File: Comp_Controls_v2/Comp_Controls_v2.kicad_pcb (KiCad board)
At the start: 2 copper layers, 35 parts

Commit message: Add edge cuts and copper fill
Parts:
- moved ANEMOMETER1 5.34 mm to (129.7, 86.0)
- moved C1 5.34 mm to (166.7, 112.7)
- moved C6 5.34 mm to (166.0, 121.6)
- moved C9 5.34 mm to (155.3, 64.3)
- moved StepDownChip1 5.34 mm to (163.7, 124.7)
- moved XBEE1 5.34 mm to (132.8, 119.8)
- moved 5V_BULK1 5.34 mm to (144.3, 48.0)
- moved TeensyC0.1 5.34 mm to (179.8, 91.1)
- moved 5V_BULK3 5.34 mm to (129.3, 48.0)
- moved 5V_MID2 5.34 mm to (125.7, 59.4)
- moved 3.3V_BULK1 5.34 mm to (178.4, 63.6)
- moved 3.3V_SYS1 5.34 mm to (179.6, 52.0)
- moved C11 5.34 mm to (146.4, 64.1)
- moved C12 5.34 mm to (163.9, 64.3)
- moved C2 5.34 mm to (166.5, 116.5)
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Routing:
- added copper zone on F.Cu, net (none)
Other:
- board outline added: 67.5 x 99 mm
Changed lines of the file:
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@@
 	(footprint "MountingHole:MountingHole_3.2mm_M3"
 		(layer "F.Cu")
-		(at 138.98 86)
+		(at 140.87 81.01)
 		(descr "Mounting Hole 3.2mm, M3, no annular, generated by kicad-footprint-generator mountinghole.py")
 		(tags "mountinghole M3")
@@
 	(footprint "Comp_Controls_v2:CAP_CL10B_01uf_0603"
 		(layer "F.Cu")
-		(at 164.6 121.44 -90)
+		(at 166.49 116.45 -90)
 		(property "Reference" "C2"
 			(at -0.21 -1.05 90)
@@
 	(footprint "Comp_Controls_v2:CAP_CL10B_01uf_0603"
 		(layer "F.Cu")
-		(at 144.54 69.05 90)
+		(at 146.43 64.06 90)
 		(property "Reference" "C11"
 			(at 1.96 -0.03 180)
@@
 	(footprint "Comp_Controls_v2:CAP_CL10B_01uf_0603"
 		(layer "F.Cu")
-		(at 148.37 126.83)
+		(at 150.26 121.84)
 		(property "Reference" "C4"
 			(at -0.21 -1.05 0)
@@
 	(footprint "Comp_Controls_v2:CAP_CL10B_01uf_0603"
 		(layer "F.Cu")
-		(at 177.9 96.06)
+		(at 179.79 91.07)
 		(property "Reference" "TeensyC0.1"
 			(at -0.21 -1.05 0)
@@
 	(footprint "Comp_Controls_v2:CAP_C3225_47uf_1210"
 		(layer "F.Cu")
-		(at 148.37 131.13 90)
+		(at 150.26 126.14 90)
 		(tags "C3225X5R1A476M250AC ")
 		(property "Reference" "C5"
@@
 			(polygon
 				(pts
-					(xy 146.973 132.1841) (xy 146.973 130.0759) (xy 149.767 130.0759) (xy 149.767 132.1841)
+					(xy 148.863 127.1941) (xy 148.863 125.0859) (xy 151.657 125.0859) (xy 151.657 127.1941)
 				)
 			)
@@
 	(footprint "Comp_Controls_v2:CAP_CL10B_01uf_0603"
 		(layer "F.Cu")
-		(at 166.36 126.52 90)
+		(at 168.25 121.53 90)
 		(property "Reference" "C3"
 			(at -2.13 0.04 180)
@@
 	(footprint "Connector_Dsub:DSUB-9_Socket_Vertical_P2.77x2.84mm_MountingHoles"
 		(layer "F.Cu")
-		(at 173.53 119.42 90)
+		(at 175.42 114.43 90)
 		(descr "9-pin D-Sub connector, straight/vertical, THT-mount, socket (female), pitch 2.77x2.84mm, distance of mounting holes 25mm, see https://disti-assets.s3.amazonaws.com/tonar/files/datasheets/16730.pdf")
 		(tags "9-pin D-Sub connector straight vertical THT socket pitch 2.77x2.84mm mounting holes distance 25mm")
@@
 	(footprint "Comp_Controls_v2:CAP_CL10B_01uf_0603"
 		(layer "F.Cu")
-		(at 164.14 126.62 90)
+		(at 166.03 121.63 90)
 		(property "Reference" "C6"
 			(at -2.03 -0.09 180)
@@
 	(footprint "MountingHole:MountingHole_3.2mm_M3"
 		(layer "F.Cu")
-		(at 157.64 137.57)
+		(at 159.53 132.58)
 		(descr "Mounting Hole 3.2mm, M3, no annular, generated by kicad-footprint-generator mountinghole.py")
 		(tags "mountinghole M3")
@@
 	(footprint "Comp_Controls_v2:CAP_CL21A_10uf_0805"
 		(layer "F.Cu")
-		(at 177.435 61.85)
+		(at 179.325 56.86)
 		(property "Reference" "3.3V_MID1"
 			(at -0.44 -1.3 0)
@@
 	(footprint "Comp_Controls_v2:CAP_CL10B_01uf_0603"
 		(layer "F.Cu")
-		(at 153.39 69.26 90)
+		(at 155.28 64.27 90)
 		(property "Reference" "C9"
 			(at 1.84 -0.07 180)
@@
 	(footprint "Comp_Controls_v2:MODULE_DEV-15583"
 		(layer "F.Cu")
-		(at 162.56 85.28 -90)
+		(at 164.45 80.29 -90)
 		(property "Reference" "TEENSY1"
 			(at -5.715 -19.685 90)
@@
 	(footprint "Comp_Controls_v2:CAP_CL10B_01uf_0603"
 		(layer "F.Cu")
-		(at 127.9 64.28 -90)
+		(at 129.79 59.29 -90)
 		(property "Reference" "5V_LOW1"
 			(at -1.98 -0.02 180)
@@
 	(footprint "Comp_Controls_v2:CAP_CL10B_01uf_0603"
 		(layer "F.Cu")
-		(at 128.27 86.02 180)
+		(at 130.16 81.03 180)
 		(property "Reference" "C10"
 			(at -0.21 -1.05 0)
@@
 	(footprint "Comp_Controls_v2:CAP_EEE1A_1000uf"
 		(layer "F.Cu")
-		(at 127.46 52.99 180)
+		(at 129.35 48 180)
 		(property "Reference" "5V_BULK3"
 			(at -0.375 -6.535 0)
@@
 	(footprint "Comp_Controls_v2:HARWIN_M20-7832046"
 		(layer "F.Cu")
-		(at 147.18 99.89)
+		(at 149.07 94.9)
 		(property "Reference" "HEADERS1"
 			(at -22.435 -3.635 0)
@@
 	(footprint "Comp_Controls_v2:CAP_CL32A_22uf_1210"
 		(layer "F.Cu")
-		(at 123.78 64.34 -90)
+		(at 125.67 59.35 -90)
 		(property "Reference" "5V_MID2"
 			(at -2.85 -0.04 180)
@@
 	(footprint "Comp_Controls_v2:XBee"
 		(layer "F.Cu")
-		(at 130.94 124.84 180)
+		(at 132.83 119.85 180)
 		(property "Reference" "XBEE1"
 			(at 0 -0.5 180)
@@
 			(polygon
 				(pts
-					(xy 145.94 140.84) (xy 120.94 140.84) (xy 120.94 104.84) (xy 145.94 104.84)
+					(xy 147.83 135.85) (xy 122.83 135.85) (xy 122.83 99.85) (xy 147.83 99.85)
 				)
 			)
@@
 	(footprint "Comp_Controls_v2:CAP_EEE1A_1000uf"
 		(layer "F.Cu")
-		(at 142.38 53 180)
+		(at 144.27 48.01 180)
 		(property "Reference" "5V_BULK1"
 			(at -0.375 -6.535 0)
@@
 	(footprint "Comp_Controls_v2:B3B-XH-A"
 		(layer "F.Cu")
-		(at 157.55 69.318333 -90)
+		(at 159.44 64.328333 -90)
 		(property "Reference" "RUDDER1"
 			(at -6.16 -0.305 180)
@@
 	(footprint "Comp_Controls_v2:B4B-XH-A"
 		(layer "F.Cu")
-		(at 127.8175 90.95)
+		(at 129.7075 85.96)
 		(property "Reference" "ANEMOMETER1"
 			(at -7.8175 0.16 90)
@@
 	(footprint "MountingHole:MountingHole_3.2mm_M3"
 		(layer "F.Cu")
-		(at 177.9 103.97)
+		(at 179.79 98.98)
 		(descr "Mounting Hole 3.2mm, M3, no annular, generated by kicad-footprint-generator mountinghole.py")
 		(tags "mountinghole M3")
@@
 	(footprint "Connector_Molex:Molex_Mini-Fit_Jr_5566-06A_2x03_P4.20mm_Vertical"
 		(layer "F.Cu")
-		(at 163.68 56.97 180)
+		(at 165.57 51.98 180)
 		(descr "Molex Mini-Fit Jr. Power Connectors, old mpn/engineering number: 5566-06A, example for new mpn: 39-28-x06x, 3 Pins per row, Mounting:  (http://www.molex.com/pdm_docs/sd/039281043_sd.pdf), generated with kicad-footprint-generator")
 		(tags "connector Molex Mini-Fit_Jr vertical")
@@
 	(footprint "Comp_Controls_v2:CAP_87510_220uf"
 		(layer "F.Cu")
-		(at 176.54 68.55 90)
+		(at 178.43 63.56 90)
 		(property "Reference" "3.3V_BULK1"
 			(at -0.6 -4.708 90)
@@
 	(footprint "Comp_Controls_v2:B3B-XH-A"
 		(layer "F.Cu")
-		(at 140.05 69.13 -90)
+		(at 141.94 64.14 -90)
 		(property "Reference" "5v_extra1"
 			(at -6.44 -0.095 180)
@@
 	(footprint "Comp_Controls_v2:MAX3323EEPE+"
 		(layer "F.Cu")
-		(at 161.85 129.65 180)
+		(at 163.74 124.66 180)
 		(tags "max3323eepe+ ")
 		(property "Reference" "StepDownChip1"
@@
 	(footprint "Comp_Controls_v2:CAP_CL10B_01uf_0603"
 		(layer "F.Cu")
-		(at 128.03 95.13 180)
+		(at 129.92 90.14 180)
 		(property "Reference" "C8"
 			(at -0.21 -1.05 0)
@@
 	(footprint "Comp_Controls_v2:B4B-XH-A"
 		(layer "F.Cu")
-		(at 127.84 81.625)
+		(at 129.73 76.635)
 		(property "Reference" "3.3v_extra1"
 			(at -7.99 -1.135 90)
@@
 	(footprint "Connector_Molex:Molex_Mini-Fit_Jr_5566-04A_2x02_P4.20mm_Vertical"
 		(layer "F.Cu")
-		(at 177.72 57.01 180)
+		(at 179.61 52.02 180)
 		(descr "Molex Mini-Fit Jr. Power Connectors, old mpn/engineering number: 5566-04A, example for new mpn: 39-28-x04x, 2 Pins per row, Mounting:  (http://www.molex.com/pdm_docs/sd/039281043_sd.pdf), generated with kicad-footprint-generator")
 		(tags "connector Molex Mini-Fit_Jr vertical")
@@
 	(footprint "Comp_Controls_v2:B3B-XH-A"
 		(layer "F.Cu")
-		(at 166.3 69.4125 -90)
+		(at 168.19 64.4225 -90)
 		(property "Reference" "SAIL1"
 			(at -6.29 0.005 180)
@@
 	(footprint "Comp_Controls_v2:CAP_CL10B_01uf_0603"
 		(layer "F.Cu")
-		(at 135.44 66.88 90)
+		(at 137.33 61.89 90)
 		(property "Reference" "C7"
 			(at 1.89 -0.02 180)
@@
 	(footprint "Comp_Controls_v2:CAP_CL10B_01uf_0603"
 		(layer "F.Cu")
-		(at 164.79 117.65 90)
+		(at 166.68 112.66 90)
 		(property "Reference" "C1"
 			(at -0.21 -1.05 90)
@@
 	(footprint "Comp_Controls_v2:B3B-XH-A"
 		(layer "F.Cu")
-		(at 148.8 69.224167 -90)
+		(at 150.69 64.234167 -90)
 		(property "Reference" "JIB1"
 			(at -6.204167 -0.06 180)
@@
 	(footprint "Comp_Controls_v2:CAP_CL10B_01uf_0603"
 		(layer "F.Cu")
-		(at 161.98 69.25 90)
+		(at 163.87 64.26 90)
 		(property "Reference" "C12"
 			(at 1.9 -0.05 180)
@@
 		(embedded_fonts no)
 	)
+	(gr_rect
+		(start 119.5 39.5)
+		(end 187 138.5)
+		(stroke
+			(width 0.05)
+			(type default)
+		)
+		(fill no)
+		(layer "Edge.Cuts")
+	)
+	(zone
+		(net 0)
+		(net_name "")
+		(layer "F.Cu")
+		(hatch edge 0.5)
+		(connect_pads
+			(clearance 0.5)
+		)
+		(min_thickness 0.25)
+		(filled_areas_thickness no)
+		(fill
+			(thermal_gap 0.5)
+			(thermal_bridge_width 0.5)
+			(island_removal_mode 1)
+			(island_area_min 10)
+		)
+		(polygon
+			(pts
+				(xy 116 36.5) (xy 190.5 36.5) (xy 190.5 142.5) (xy 116.5 142.5)
+			)
+		)
+	)
 	(embedded_fonts no)

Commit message: finished ground vias
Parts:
- moved C2 4.27 mm to (166.3, 112.2), turned to 90 degrees
- moved C1 3.38 mm to (166.0, 116.0)
- renumbered JIB1 to JIB, RUDDER1 to RUDDER, SAIL1 to SAIL
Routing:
- net GND: track 0.00 -> 23.5 mm, vias 0 -> 16
- net Net-(VectorNavInput1-Pad1): track 0.00 -> 11.5 mm
- net Net-(StepDownChip1-C1+): track 0.00 -> 5.48 mm
- net Net-(StepDownChip1-C1-): track 0.00 -> 4.99 mm
- net Net-(StepDownChip1-V-): track 0.00 -> 3.00 mm
- net Net-(StepDownChip1-V+): track 0.00 -> 2.82 mm
- net Net-(StepDownChip1-C2-): track 0.00 -> 2.53 mm
- net Net-(StepDownChip1-C2+): track 0.00 -> 2.36 mm

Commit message: Add tracks
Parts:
- moved C8 1.74 mm to (128.2, 90.5)
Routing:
- net WindData1: track 0.00 -> 40.1 mm
- net WindData0: track 0.00 -> 35.0 mm
- net 5v_extra: track 0.00 -> 26.8 mm
- net Extra41: track 0.00 -> 23.9 mm
- net Extra40: track 0.00 -> 18.8 mm
- net Rudder: track 0.00 -> 11.8 mm
- net JIB: track 0.00 -> 8.17 mm
- net Sail: track 0.00 -> 7.29 mm
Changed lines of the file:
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@@
 	(footprint "Comp_Controls_v2:CAP_CL10B_01uf_0603"
 		(layer "F.Cu")
-		(at 129.92 90.14 180)
+		(at 128.22 90.5 180)
 		(property "Reference" "C8"
 			(at -0.21 -1.05 0)
@@
 	)
 	(segment
-		(start 129.14 90.14)
-		(end 128.13 90.14)
+		(start 127.44 90.5)
+		(end 126.43 90.5)
 		(width 0.2)
 		(layer "F.Cu")
@@
 	)
 	(segment
-		(start 128.13 90.14)
-		(end 128.12 90.15)
+		(start 126.43 90.5)
+		(end 126.42 90.51)
 		(width 0.2)
 		(layer "F.Cu")
@@
 	)
 	(via
-		(at 128.12 90.15)
+		(at 126.42 90.51)
 		(size 0.6)
 		(drill 0.3)
@@
 	)
 	(segment
+		(start 131.904 73.736)
+		(end 149.414 73.736)
+		(width 0.2)
+		(layer "F.Cu")
+		(net 3)
+	)
+	(segment
+		(start 149.414 73.736)
+		(end 150.48 72.67)
+		(width 0.2)
+		(layer "F.Cu")
+		(net 3)
+	)
+	(segment
+		(start 128.48 77.16)
+		(end 131.904 73.736)
+		(width 0.2)
+		(layer "F.Cu")
+		(net 3)
+	)
+	(segment
+		(start 130.98 77.16)
+		(end 135.47 72.67)
+		(width 0.2)
+		(layer "B.Cu")
+		(net 4)
+	)
+	(segment
+		(start 135.47 72.67)
+		(end 147.94 72.67)
+		(width 0.2)
+		(layer "B.Cu")
+		(net 4)
+	)
+	(segment
+		(start 163.55 70.5)
+		(end 165.72 72.67)
+		(width 0.2)
+		(layer "F.Cu")
+		(net 7)
+	)
+	(segment
+		(start 143.14 66.64)
+		(end 147 70.5)
+		(width 0.2)
+		(layer "F.Cu")
+		(net 7)
+	)
+	(segment
+		(start 141.415 66.64)
+		(end 143.14 66.64)
+		(width 0.2)
+		(layer "F.Cu")
+		(net 7)
+	)
+	(segment
+		(start 147 70.5)
+		(end 163.55 70.5)
+		(width 0.2)
+		(layer "F.Cu")
+		(net 7)
+	)
+	(segment
+		(start 134.9725 90.5)
+		(end 149.75 90.5)
+		(width 0.2)
+		(layer "B.Cu")
+		(net 8)
+	)
+	(segment
+		(start 156.01 90.5)
+		(end 158.05 90.5)
+		(width 0.2)
+		(layer "B.Cu")
+		(net 8)
+	)
+	(segment
+		(start 149.75 90.5)
+		(end 152.88 93.63)
+		(width 0.2)
+		(layer "B.Cu")
+		(net 8)
+	)
+	(segment
+		(start 130.9575 86.485)
+		(end 134.9725 90.5)
+		(width 0.2)
+		(layer "B.Cu")
+		(net 8)
+	)
+	(segment
+		(start 158.05 90.5)
+		(end 160.64 87.91)
+		(width 0.2)
+		(layer "B.Cu")
+		(net 8)
+	)
+	(segment
+		(start 152.88 93.63)
+		(end 156.01 90.5)
+		(width 0.2)
+		(layer "B.Cu")
+		(net 8)
+	)
+	(segment
+		(start 159.59 91.5)
+		(end 163.18 87.91)
+		(width 0.2)
+		(layer "F.Cu")
+		(net 9)
+	)
+	(segment
+		(start 153.29 91.5)
+		(end 155.42 93.63)
+		(width 0.2)
+		(layer "F.Cu")
+		(net 9)
+	)
+	(segment
+		(start 157.5 91.5)
+		(end 159.59 91.5)
+		(width 0.2)
+		(layer "F.Cu")
+		(net 9)
+	)
+	(segment
+		(start 157.5 91.55)
+		(end 157.5 91.5)
+		(width 0.2)
+		(layer "F.Cu")
+		(net 9)
+	)
+	(segment
+		(start 128.4575 86.485)
+		(end 133.4725 91.5)
+		(width 0.2)
+		(layer "F.Cu")
+		(net 9)
+	)
+	(segment
+		(start 133.4725 91.5)
+		(end 153.29 91.5)
+		(width 0.2)
+		(layer "F.Cu")
+		(net 9)
+	)
+	(segment
+		(start 155.42 93.63)
+		(end 157.5 91.55)
+		(width 0.2)
+		(layer "F.Cu")
+		(net 9)
+	)
+	(segment
 		(start 164.03 116.75)
 		(end 163.74 117.04)
@@
 	)
 	(segment
+		(start 164.5 70.5)
+		(end 166.09 70.5)
+		(width 0.2)
+		(layer "F.Cu")
+		(net 18)
+	)
+	(segment
+		(start 160.828333 66.828333)
+		(end 164.5 70.5)
+		(width 0.2)
+		(layer "F.Cu")
+		(net 18)
+	)
+	(segment
+		(start 166.09 70.5)
+		(end 168.26 72.67)
+		(width 0.2)
+		(layer "F.Cu")
+		(net 18)
+	)
+	(segment
+		(start 158.915 66.828333)
+		(end 160.828333 66.828333)
+		(width 0.2)
+		(layer "F.Cu")
+		(net 18)
+	)
+	(segment
+		(start 167.2425 66.5)
+		(end 167 66.5)
+		(width 0.2)
+		(layer "F.Cu")
+		(net 29)
+	)
+	(segment
+		(start 167.665 69.535)
+		(end 170.8 72.67)
+		(width 0.2)
+		(layer "B.Cu")
+		(net 29)
+	)
+	(segment
+		(start 167.665 66.9225)
+		(end 167.665 69.535)
+		(width 0.2)
+		(layer "B.Cu")
+		(net 29)
+	)
+	(segment
+		(start 150.165 66.734167)
+		(end 150.165 67.275)
+		(width 0.2)
+		(layer "B.Cu")
+		(net 32)
+	)
+	(segment
+		(start 150.165 67.275)
+		(end 155.56 72.67)
+		(width 0.2)
+		(layer "B.Cu")
+		(net 32)
+	)
+	(segment

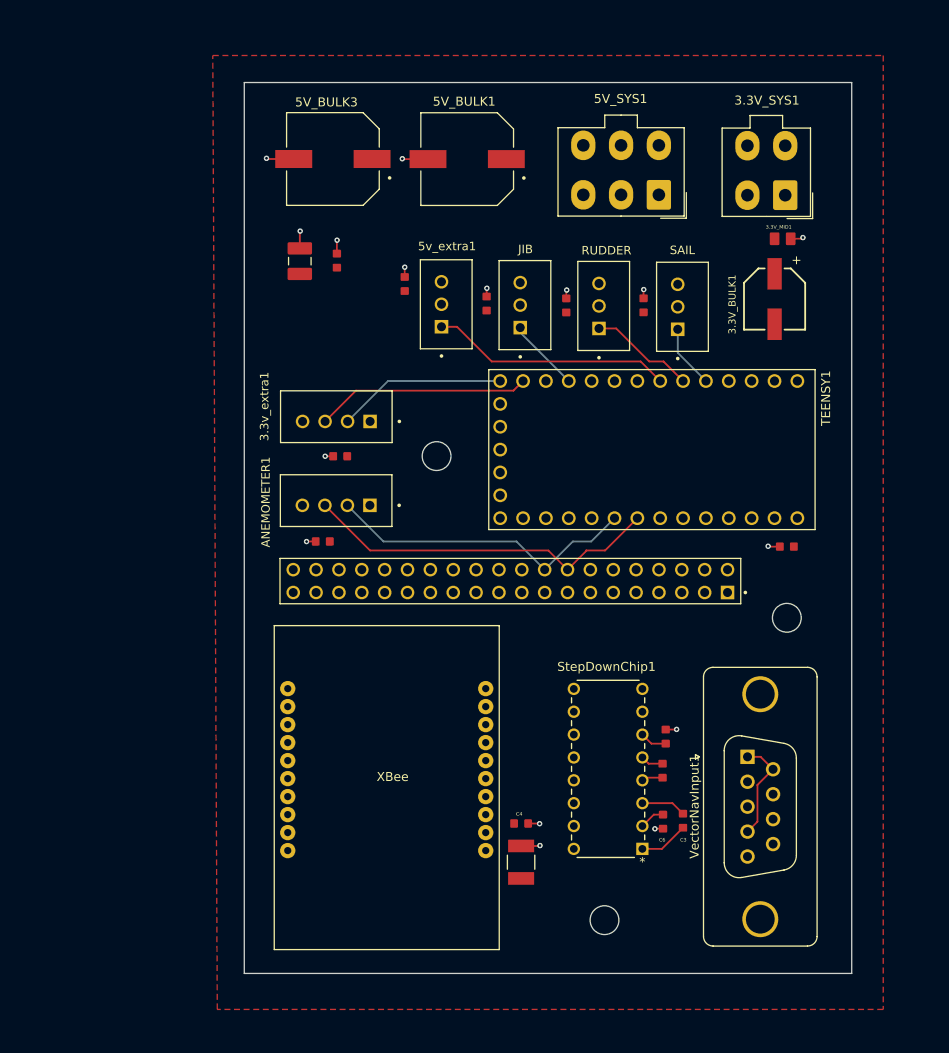
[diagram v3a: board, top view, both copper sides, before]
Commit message: changed mounting holes
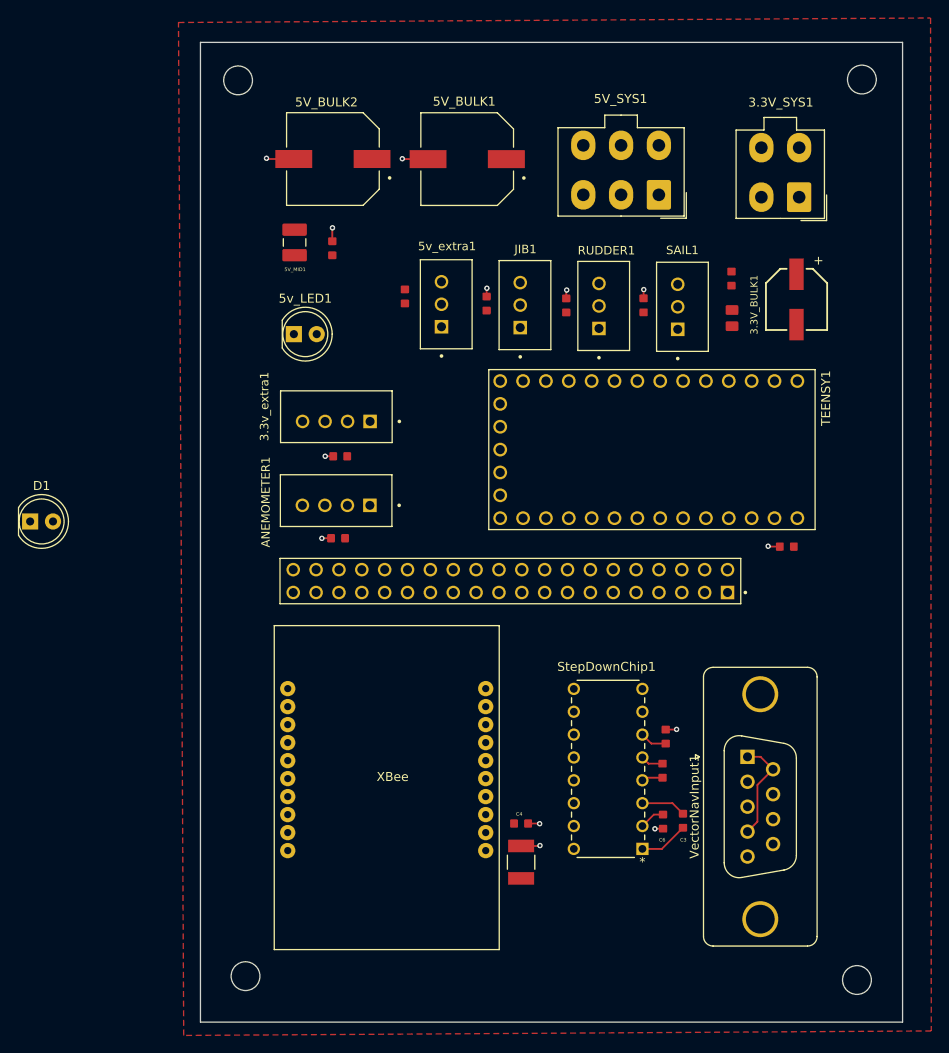
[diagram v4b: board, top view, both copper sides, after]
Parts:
- removed 5V_MID2: 22uf, Comp_Controls_v2:CAP_CL32A_22uf_1210
- added 3.3V_LOW1: 0.1uf, Comp_Controls_v2:CAP_CL10B_01uf_0603, F.Cu at (173.6, 61.3)
- added 5V_MID1: 22uf, Comp_Controls_v2:CAP_CL32A_22uf_1210, F.Cu at (125.1, 57.3)
- added 5v_LED1: 5v_LED, LED_THT:LED_D5.0mm, F.Cu at (125.0, 67.5)
- added D1: 3.3v_LED, LED_THT:LED_D5.0mm, F.Cu at (95.7, 88.3)
- added H4: MountingHole, MountingHole:MountingHole_3.2mm_M3, F.Cu at (188.1, 39.2)
- moved H2 47.2 mm to (118.8, 39.3)
- moved H1 41.0 mm to (187.6, 139.2)
- moved H3 40.4 mm to (119.6, 138.8)
- moved 3.3V_MID1 10.5 mm to (173.7, 65.7), turned to -90 degrees
- moved 3.3V_BULK1 2.44 mm to (180.9, 63.6)
- moved C8 1.74 mm to (129.9, 90.1)
- moved 3.3V_SYS1 1.57 mm to (181.2, 52.2)
- moved 5V_LOW1 1.46 mm to (129.3, 57.9)
- moved C7 1.38 mm to (137.3, 63.3)
- renumbered 5V_BULK3 to 5V_BULK2, JIB to JIB1, RUDDER to RUDDER1, SAIL to SAIL1
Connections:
- net 5.5v_extra renamed 3.3v_extra
- 5v_extra1 pad 2: +5V_SYS2 -> +5V_SYS1
- C7 pad 1: +5V_SYS2 -> +5V_SYS1
- C9 pad 1: +5V_SYS2 -> +5V_SYS1
- RUDDER1 pad 2: +5V_SYS2 -> +5V_SYS1
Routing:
- net WindData1: track 40.1 -> 0.00 mm
- net WindData0: track 35.0 -> 0.00 mm
- net 5v_extra: track 26.8 -> 0.00 mm
- net Extra41: track 23.9 -> 0.00 mm
- net Extra40: track 18.8 -> 0.00 mm
- net Rudder: track 11.8 -> 0.00 mm
- net JIB: track 8.17 -> 0.00 mm
- net Sail: track 7.29 -> 0.00 mm
- net GND: track 23.5 -> 19.1 mm, vias 16 -> 13
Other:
- board size 67.5 x 99 mm -> 78 x 108.9 mm

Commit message: move LED
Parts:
- moved D1 45.3 mm to (140.1, 79.6)
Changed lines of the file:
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@@
 	(footprint "LED_THT:LED_D5.0mm"
 		(layer "F.Cu")
-		(at 95.705 88.275)
+		(at 140.135 79.59)
 		(descr "LED, diameter 5.0mm, 2 pins, http://cdn-reichelt.de/documents/datenblatt/A500/LL-504BC2E-009.pdf, generated by kicad-footprint-generator")
 		(tags "LED")
